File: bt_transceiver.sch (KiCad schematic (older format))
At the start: 6 parts, among them U3 RN42

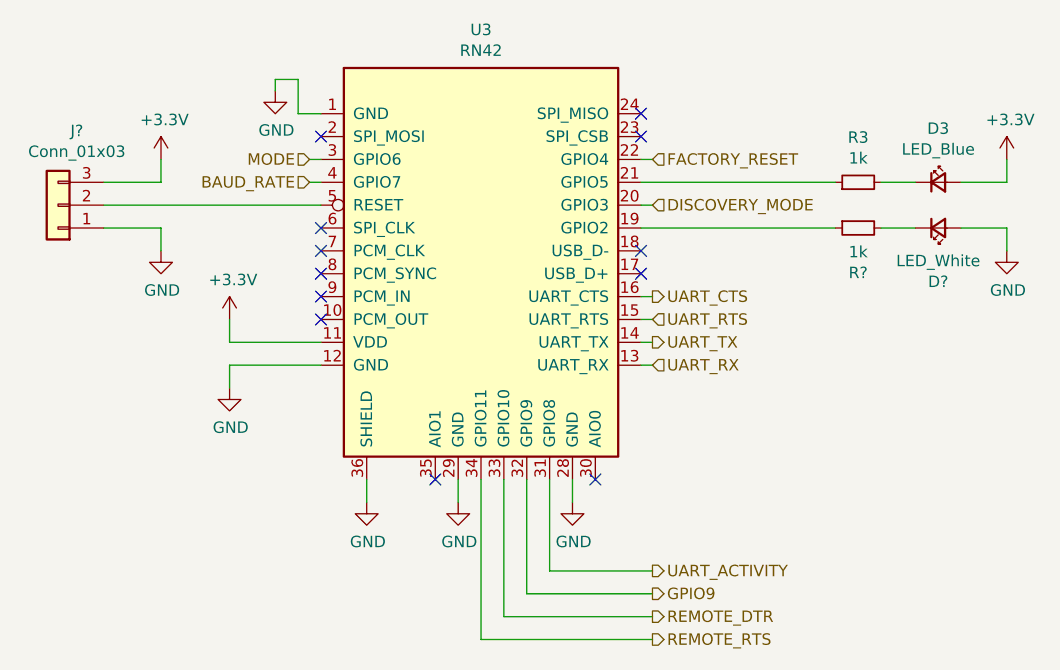
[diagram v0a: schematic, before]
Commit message: Updated footprints
Updated some parts to JLCPCB SMT library and also added some footprints
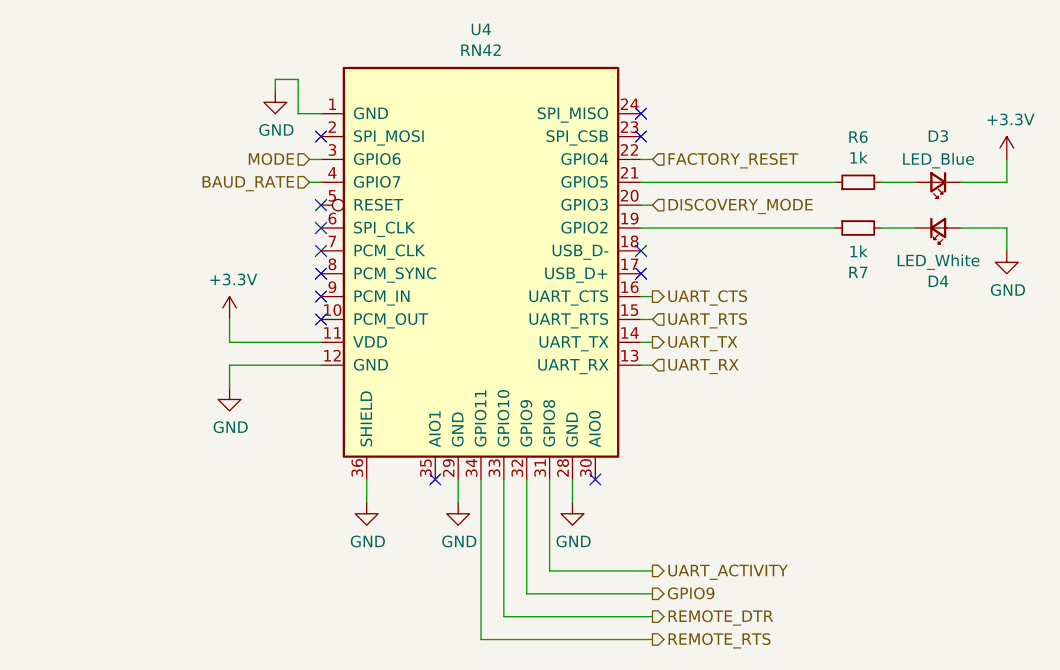
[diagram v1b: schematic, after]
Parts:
- removed J?: Conn_01x03, symbol Connector_Generic:Conn_01x03
- D3: footprint (none) -> LED_SMD:LED_0603_1608Metric
- D4: renamed from D?; footprint (none) -> LED_SMD:LED_0603_1608Metric
- gave numbers to parts that had none: 1
- renumbered R3 to R6, U3 to U4
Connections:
- net +3V3: now also D3.1 (K); no longer D3.2 (A)
- net at R6.2: now also D3.2 (A); no longer D3.1 (K)
- no-connect marks 12 -> 13
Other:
- moved on the sheet: D3
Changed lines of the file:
@@
 $Descr A4 11693 8268
 encoding utf-8
-Sheet 4 4
+Sheet 3 4
 Title "MP3 Player"
 Date "2021-02-28"
@@
 $EndDescr
 $Comp
-L RF_Bluetooth:RN42 U3
+L RF_Bluetooth:RN42 U4
 U 1 1 60CA4A22
 P 5800 3950
-F 0 "U3" H 5800 5017 50  0000 C CNN
+F 0 "U4" H 5800 5017 50  0000 C CNN
 F 1 "RN42" H 5800 4926 50  0000 C CNN
 F 2 "RF_Module:RN42" H 5750 4800 50  0001 C CNN
@@
 NoConn ~ 6500 3950
 $Comp
-L Device:R_Small R3
+L Device:R_Small R6
 U 1 1 60CA4A67
 P 7450 3550
-F 0 "R3" V 7646 3550 50  0000 C CNN
+F 0 "R6" V 7646 3550 50  0000 C CNN
 F 1 "1k" V 7555 3550 50  0000 C CNN
 F 2 "" H 7450 3550 50  0001 C CNN
@@
 U 1 1 60CA4A6E
 P 7800 3550
-F 0 "D3" H 7800 3785 50  0000 C CNN
-F 1 "LED_Blue" H 7800 3694 50  0000 C CNN
-F 2 "" V 7800 3550 50  0001 C CNN
+F 0 "D3" H 7800 3350 50  0000 C CNN
+F 1 "LED_Blue" H 7800 3450 50  0000 C CNN
+F 2 "LED_SMD:LED_0603_1608Metric" V 7800 3550 50  0001 C CNN
 F 3 "~" V 7800 3550 50  0001 C CNN
 	1    7800 3550
-	1    0    0    -1
+	-1   0    0    1
 $EndComp
 Wire Wire Line
 	7700 3550 7550 3550
 $Comp
-L power:+3.3V #PWR0114
+L power:+3.3V #PWR025
 U 1 1 60CA4A75
 P 8100 3450
-F 0 "#PWR0114" H 8100 3300 50  0001 C CNN
+F 0 "#PWR025" H 8100 3300 50  0001 C CNN
 F 1 "+3.3V" H 8115 3623 50  0000 C CNN
 F 2 "" H 8100 3450 50  0001 C CNN
@@
 UART_RX
 $Comp
-L power:+3.3V #PWR?
+L power:+3.3V #PWR019
 U 1 1 60488D4F
 P 4700 4150
-F 0 "#PWR?" H 4700 4000 50  0001 C CNN
+F 0 "#PWR019" H 4700 4000 50  0001 C CNN
 F 1 "+3.3V" H 4715 4323 50  0000 C CNN
 F 2 "" H 4700 4150 50  0001 C CNN
@@
 	4700 4250 5100 4250
 $Comp
-L power:GND #PWR?
+L power:GND #PWR020
 U 1 1 60489CE5
 P 4700 4450
-F 0 "#PWR?" H 4700 4200 50  0001 C CNN
+F 0 "#PWR020" H 4700 4200 50  0001 C CNN
 F 1 "GND" H 4705 4277 50  0000 C CNN
 F 2 "" H 4700 4450 50  0001 C CNN
@@
 	4700 4350 5100 4350
 $Comp
-L power:GND #PWR?
+L power:GND #PWR022
 U 1 1 6048A6BC
 P 5300 4950
-F 0 "#PWR?" H 5300 4700 50  0001 C CNN
+F 0 "#PWR022" H 5300 4700 50  0001 C CNN
 F 1 "GND" H 5305 4777 50  0000 C CNN
 F 2 "" H 5300 4950 50  0001 C CNN
@@
 $EndComp
 $Comp
-L power:GND #PWR?
+L power:GND #PWR023
 U 1 1 6048A79A
 P 5700 4950
-F 0 "#PWR?" H 5700 4700 50  0001 C CNN
+F 0 "#PWR023" H 5700 4700 50  0001 C CNN
 F 1 "GND" H 5705 4777 50  0000 C CNN
 F 2 "" H 5700 4950 50  0001 C CNN
@@
 $EndComp
 $Comp
-L power:GND #PWR?
+L power:GND #PWR024
 U 1 1 6048A98E
 P 6200 4950
-F 0 "#PWR?" H 6200 4700 50  0001 C CNN
+F 0 "#PWR024" H 6200 4700 50  0001 C CNN
 F 1 "GND" H 6205 4777 50  0000 C CNN
 F 2 "" H 6200 4950 50  0001 C CNN
@@
 	5050 3550 5100 3550
 $Comp
-L Connector_Generic:Conn_01x03 J?
-U 1 1 6048C459
-P 3950 3650
-F 0 "J?" H 3868 3325 50  0000 C CNN
-F 1 "Conn_01x03" H 3868 3416 50  0000 C CNN
-F 2 "" H 3950 3650 50  0001 C CNN
-F 3 "~" H 3950 3650 50  0001 C CNN
-	1    3950 3650
-	-1   0    0    1
-$EndComp
-Wire Wire Line
-	4150 3650 5100 3650
-$Comp
-L power:+3.3V #PWR?
-U 1 1 6048CE20
-P 4400 3450
-F 0 "#PWR?" H 4400 3300 50  0001 C CNN
-F 1 "+3.3V" H 4415 3623 50  0000 C CNN
-F 2 "" H 4400 3450 50  0001 C CNN
-F 3 "" H 4400 3450 50  0001 C CNN
-	1    4400 3450
-	1    0    0    -1
-$EndComp
-Wire Wire Line
-	4400 3450 4400 3550
-Wire Wire Line
-	4400 3550 4150 3550
-$Comp
-L power:GND #PWR?
-U 1 1 6048D63F
-P 4400 3850
-F 0 "#PWR?" H 4400 3600 50  0001 C CNN
-F 1 "GND" H 4405 3677 50  0000 C CNN
-F 2 "" H 4400 3850 50  0001 C CNN
-F 3 "" H 4400 3850 50  0001 C CNN
-	1    4400 3850
-	1    0    0    -1
-$EndComp
-Wire Wire Line
-	4400 3850 4400 3750
-Wire Wire Line
-	4400 3750 4150 3750
-$Comp
-L power:GND #PWR?
+L power:GND #PWR021
 U 1 1 6048DF6B
 P 4900 3150
-F 0 "#PWR?" H 4900 2900 50  0001 C CNN
+F 0 "#PWR021" H 4900 2900 50  0001 C CNN
 F 1 "GND" H 4905 2977 50  0000 C CNN
 F 2 "" H 4900 3150 50  0001 C CNN
@@
 	5000 3250 5100 3250
 $Comp
-L Device:R_Small R?
+L Device:R_Small R7
 U 1 1 60492B5E
 P 7450 3750
-F 0 "R?" V 7646 3750 50  0000 C CNN
+F 0 "R7" V 7646 3750 50  0000 C CNN
 F 1 "1k" V 7555 3750 50  0000 C CNN
 F 2 "" H 7450 3750 50  0001 C CNN
@@
 $EndComp
 $Comp
-L Device:LED_Small D?
+L Device:LED_Small D4
 U 1 1 60492D63
 P 7800 3750
-F 0 "D?" H 7800 3985 50  0000 C CNN
+F 0 "D4" H 7800 3985 50  0000 C CNN
 F 1 "LED_White" H 7800 3894 50  0000 C CNN
-F 2 "" V 7800 3750 50  0001 C CNN
+F 2 "LED_SMD:LED_0603_1608Metric" V 7800 3750 50  0001 C CNN
 F 3 "~" V 7800 3750 50  0001 C CNN
 	1    7800 3750
@@
 GPIO9
 $Comp
-L power:GND #PWR?
+L power:GND #PWR026
 U 1 1 6052D0AA
 P 8100 3850
-F 0 "#PWR?" H 8100 3600 50  0001 C CNN
+F 0 "#PWR026" H 8100 3600 50  0001 C CNN
 F 1 "GND" H 8105 3677 50  0000 C CNN
 F 2 "" H 8100 3850 50  0001 C CNN
@@
 Wire Wire Line
 	8100 3850 8100 3750
+NoConn ~ 5100 3650
 $EndSCHEMATC

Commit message: Update footprints
Add footprints for resistors, push buttons, regulator, and crystals
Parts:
- R6, R7: footprint (none) -> Resistor_SMD:R_0603_1608Metric
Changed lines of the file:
@@
 F 0 "R6" V 7646 3550 50  0000 C CNN
 F 1 "1k" V 7555 3550 50  0000 C CNN
-F 2 "" H 7450 3550 50  0001 C CNN
+F 2 "Resistor_SMD:R_0603_1608Metric" H 7450 3550 50  0001 C CNN
 F 3 "~" H 7450 3550 50  0001 C CNN
 	1    7450 3550
@@
 F 0 "R7" V 7646 3750 50  0000 C CNN
 F 1 "1k" V 7555 3750 50  0000 C CNN
-F 2 "" H 7450 3750 50  0001 C CNN
+F 2 "Resistor_SMD:R_0603_1608Metric" H 7450 3750 50  0001 C CNN
 F 3 "~" H 7450 3750 50  0001 C CNN
 	1    7450 3750
